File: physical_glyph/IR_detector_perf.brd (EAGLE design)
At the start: 100 x 80 mm, 31 parts, among them IC1 7805T, T1 BP103, U1 MCP6004-I/P, U2 LM339PWR

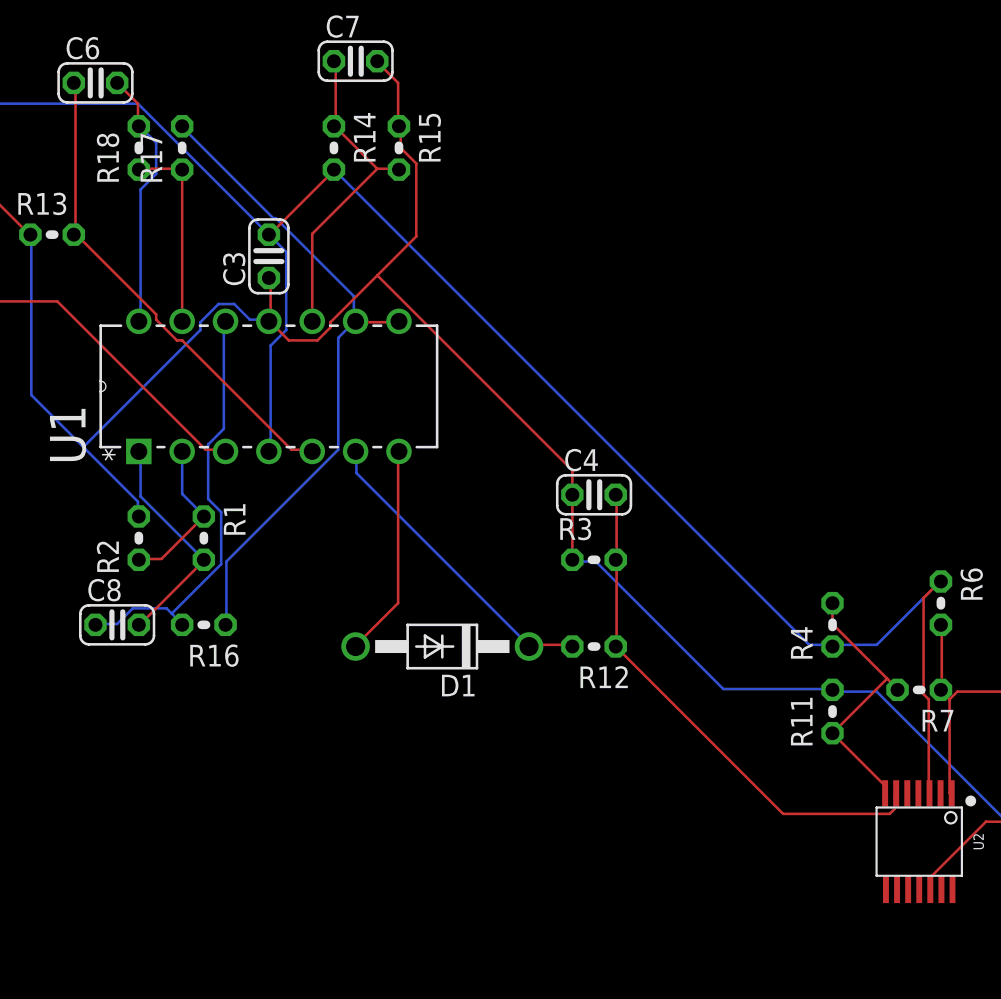
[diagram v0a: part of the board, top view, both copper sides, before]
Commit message: Simplify all resistors and clarify comparator resistors
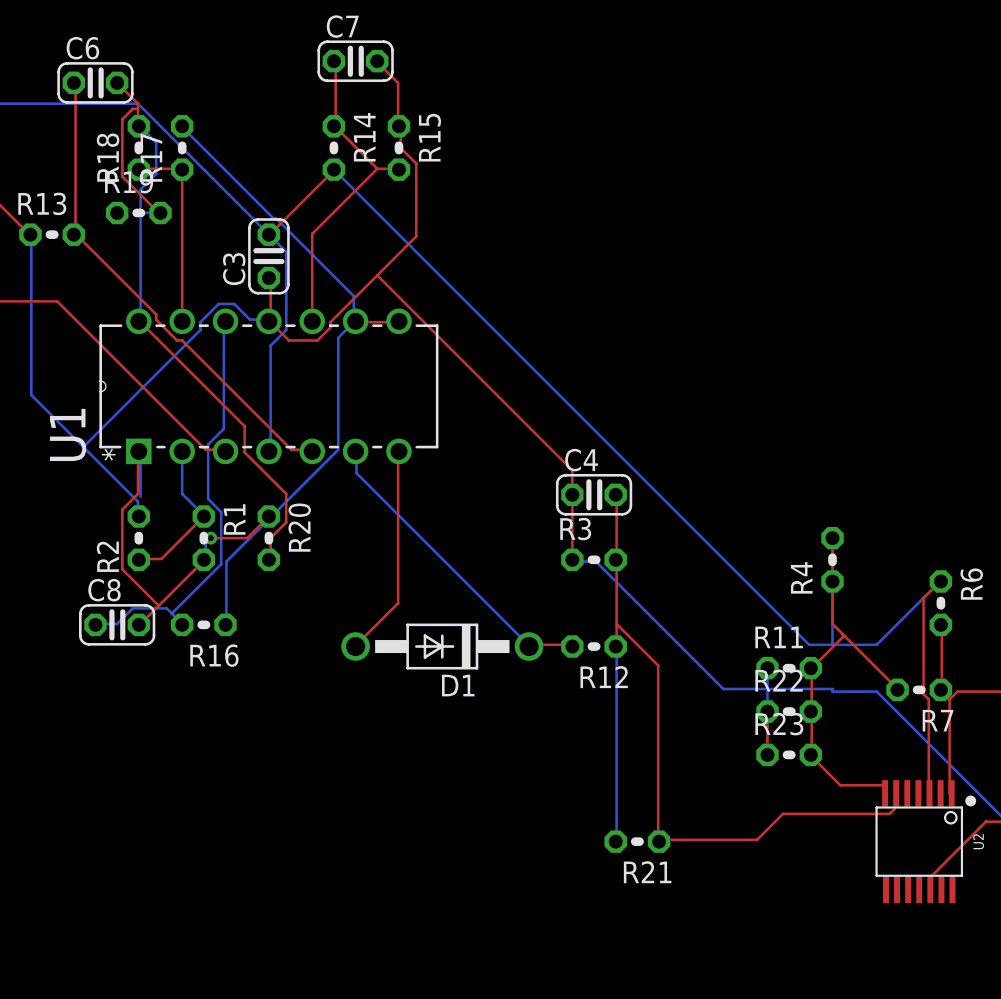
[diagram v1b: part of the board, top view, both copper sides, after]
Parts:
- added R19, R20: 4.7k, rcl:0204V
- added R21: 1k, rcl:0204V
- added R22, R23: 1M, rcl:0204V
- R1, R18: value 14.7k -> 10k
- R11: value 333333 -> 1M
- R12: value 2k -> 1k
- moved R4 3.81 mm to (80.0, 44.5)
- moved R11 3.59 mm to (77.5, 38.1), turned to 0 degrees
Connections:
- new net N$6: R18.2, R19.1
- new net N$7: R1.2, R20.1
- new net N$8: R12.1, R21.2
- net GAIN2_OUT: now also R19.2, R20.2; no longer R18.2
- net GAIN_OUT: no longer R1.2
- net GND: now also R11.1, R22.1, R23.1; no longer R11.2
- net N$34: now also R11.2, R22.2, R23.2; no longer R11.1
- net PEAK_OUT: now also R21.1; no longer R12.1
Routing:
- net GAIN2_OUT: track 15.3 -> 41.9 mm
- net N$8: track 0.00 -> 11.5 mm
- net N$34: track 16.0 -> 24.5 mm
- net PEAK_OUT: track 30.4 -> 38.1 mm
- net N$7: track 0.00 -> 5.39 mm, vias 0 -> 1
- net GND: track 169.1 -> 174.2 mm
- net GAIN_OUT: track 13.3 -> 18.3 mm
- net 5V: track 139.0 -> 142.6 mm

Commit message: Final edits and fixes to IR detector circuit
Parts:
- added C9: 0.1uF, resistor:C025-024X044
- moved R21 13.3 mm to (64.8, 40.6), turned to 90 degrees
- moved R12 5.24 mm to (64.8, 44.5), turned to 270 degrees
- moved C4 5.08 mm to (66.0, 53.3)
- moved R3 5.08 mm to (66.0, 49.5)
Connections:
- net 5V: now also C9.2
- net GAIN2_OUT: no longer R20.2
- net GAIN_OUT: now also R20.2
- net GND: now also C9.1
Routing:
- net PEAK_OUT: track 38.1 -> 77.8 mm
- net N$8: track 11.5 -> 32.3 mm
- net 5V: track 142.6 -> 159.2 mm
- net GAIN_OUT: track 18.3 -> 29.9 mm
- net GND: track 174.2 -> 182.8 mm
- net PEAK_DIODE: track 18.3 -> 21.9 mm
